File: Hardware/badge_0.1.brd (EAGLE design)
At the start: 100 x 50 mm, 59 parts, among them CON1 PH_2, IC1 CP2102, SW2 MK12C02, U1 SMBT2222A, U2 SMBT2222A, U4 MCP73832T-2DCI/OT

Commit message: Added optional connections to the anchors for the battery connector and slide switch To place on schematic, use the invoke tool
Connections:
- net GND: now also CON1.P$3, CON1.P$4, SW2.P$4, SW2.P$5, SW2.P$6, SW2.P$7
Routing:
- net GND: track 372.4 -> 379.8 mm, vias 114 -> 117
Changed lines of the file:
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@@
 <?xml version="1.0" encoding="utf-8"?>
 <!DOCTYPE eagle SYSTEM "eagle.dtd">
-<eagle version="7.5.0">
+<eagle version="7.1.0">
 <drawing>
 <settings>
@@
 <via x="48.10125" y="28.09875" extent="1-16" drill="0.4064" diameter="0.8128" shape="octagon"/>
 <wire x1="48.10125" y1="28.09875" x2="49.05375" y2="28.09875" width="0.8128" layer="1"/>
-<wire x1="61.595" y1="34.6075" x2="60.563125" y2="34.6075" width="0.8128" layer="1"/>
-<via x="60.563125" y="34.6075" extent="1-16" drill="0.635" shape="octagon"/>
-<wire x1="60.563125" y1="34.6075" x2="61.43625" y2="34.6075" width="0.8128" layer="16"/>
+<wire x1="61.595" y1="34.6075" x2="61.198125" y2="34.6075" width="0.8128" layer="1"/>
+<via x="61.198125" y="34.6075" extent="1-16" drill="0.635" shape="octagon"/>
+<wire x1="61.198125" y1="34.6075" x2="61.43625" y2="34.6075" width="0.8128" layer="16"/>
 <wire x1="61.43625" y1="34.6075" x2="61.595" y2="34.44875" width="0.8128" layer="16"/>
 <wire x1="74.93" y1="26.19375" x2="74.93" y2="22.70125" width="0.8128" layer="16"/>
 <via x="67.706875" y="6.985" extent="1-16" drill="0.635" shape="octagon"/>
-<polygon width="0.3048" layer="1" thermals="no">
-<vertex x="65.960625" y="10.00125"/>
-<vertex x="68.341875" y="10.00125"/>
-<vertex x="68.341875" y="6.429375"/>
-<vertex x="65.88125" y="6.429375"/>
-</polygon>
 <polygon width="0.254" layer="1">
 <vertex x="92.86875" y="44.92625"/>
@@
 <via x="9.128125" y="33.17875" extent="1-16" drill="0.635" shape="octagon"/>
 <wire x1="9.128125" y1="33.17875" x2="15.08125" y2="33.17875" width="0.8128" layer="16"/>
+<polygon width="0.3048" layer="1" isolate="0.2032" thermals="no" rank="2">
+<vertex x="0.238125" y="44.45"/>
+<vertex x="0.238125" y="35.56"/>
+<vertex x="5.87375" y="35.56"/>
+<vertex x="5.87375" y="44.45"/>
+</polygon>
+<contactref element="CON1" pad="P$3"/>
+<contactref element="CON1" pad="P$4"/>
+<polygon width="0.3048" layer="1" isolate="0.254" thermals="no" rank="3">
+<vertex x="61.198125" y="0.714375"/>
+<vertex x="61.198125" y="10.080625"/>
+<vertex x="69.37375" y="10.080625"/>
+<vertex x="69.37375" y="0.714375"/>
+</polygon>
+<contactref element="SW2" pad="P$4"/>
+<contactref element="SW2" pad="P$5"/>
+<contactref element="SW2" pad="P$6"/>
+<contactref element="SW2" pad="P$7"/>
+<wire x1="9.04875" y1="47.9425" x2="8.969375" y2="47.9425" width="0.3048" layer="1"/>
+<wire x1="8.969375" y1="47.9425" x2="7.46125" y2="46.434375" width="0.3048" layer="1"/>
+<wire x1="7.46125" y1="46.434375" x2="4.048125" y2="46.434375" width="0.3048" layer="1"/>
+<wire x1="4.048125" y1="46.434375" x2="3.01625" y2="45.4025" width="0.3048" layer="1"/>
+<wire x1="3.01625" y1="45.4025" x2="3.01625" y2="43.97375" width="0.3048" layer="1"/>
+<wire x1="3.01625" y1="43.97375" x2="3.095625" y2="43.894375" width="0.3048" layer="1"/>
+<via x="68.8975" y="6.985" extent="1-16" drill="0.635" shape="octagon"/>
+<via x="68.8975" y="8.255" extent="1-16" drill="0.635" shape="octagon"/>
+<via x="68.8975" y="9.525" extent="1-16" drill="0.635" shape="octagon"/>
 </signal>
 <signal name="GPIO12/SPI_SO">

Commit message: removed slant from lcd reset trace upon Yu Siang's rec
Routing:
- net RESET: track 178.0 -> 155.9 mm
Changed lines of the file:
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@@
 <?xml version="1.0" encoding="utf-8"?>
 <!DOCTYPE eagle SYSTEM "eagle.dtd">
-<eagle version="7.1.0">
+<eagle version="7.5.0">
 <drawing>
 <settings>
@@
 <contactref element="TP5" pad="TP"/>
 <via x="11.985625" y="21.11375" extent="1-16" drill="0.3048" shape="octagon"/>
-<wire x1="7.858" y1="19.98175" x2="9.035" y2="21.15875" width="0.3048" layer="1"/>
-<wire x1="7.858" y1="19.98175" x2="5.23875" y2="19.98175" width="0.3048" layer="1"/>
 <wire x1="5.23875" y1="27.4350625" x2="4.4163125" y2="27.4350625" width="0.3048" layer="1"/>
 <wire x1="4.4163125" y1="27.4350625" x2="4.1275" y2="27.14625" width="0.3048" layer="1"/>
@@
 <wire x1="53.2844375" y1="39.14775" x2="56.29275" y2="39.14775" width="0.3048" layer="1"/>
 <wire x1="56.29275" y1="39.14775" x2="57.070625" y2="39.925625" width="0.3048" layer="1"/>
-<wire x1="11.985625" y1="21.11375" x2="11.985625" y2="13.414375" width="0.4064" layer="1"/>
-<wire x1="11.985625" y1="13.414375" x2="16.271875" y2="9.128125" width="0.4064" layer="1"/>
-<wire x1="16.271875" y1="9.128125" x2="35.639375" y2="9.128125" width="0.4064" layer="1"/>
-<wire x1="35.639375" y1="9.128125" x2="36.83" y2="10.31875" width="0.4064" layer="1"/>
-<via x="36.83" y="10.31875" extent="1-16" drill="0.6" shape="square"/>
-<wire x1="36.83" y1="10.31875" x2="36.83" y2="27.543125" width="0.4064" layer="16"/>
 <wire x1="36.83" y1="27.543125" x2="35.56" y2="28.813125" width="0.4064" layer="16"/>
 <wire x1="35.56" y1="28.813125" x2="35.56" y2="29.606875" width="0.4064" layer="16"/>
@@
 <wire x1="57.070625" y1="39.925625" x2="57.070625" y2="40.64" width="0.3048" layer="1"/>
 <wire x1="57.070625" y1="40.64" x2="56.99125" y2="40.719375" width="0.3048" layer="1"/>
+<wire x1="9.035" y1="21.15875" x2="6.41575" y2="21.15875" width="0.4064" layer="1"/>
+<wire x1="6.41575" y1="21.15875" x2="5.23875" y2="19.98175" width="0.4064" layer="1"/>
+<wire x1="11.985625" y1="21.11375" x2="15.08125" y2="21.11375" width="0.4064" layer="1"/>
+<wire x1="15.08125" y1="21.11375" x2="16.271875" y2="22.304375" width="0.4064" layer="1"/>
+<wire x1="16.271875" y1="22.304375" x2="16.271875" y2="24.050625" width="0.4064" layer="1"/>
+<wire x1="16.271875" y1="24.050625" x2="17.4625" y2="25.24125" width="0.4064" layer="1"/>
+<wire x1="17.4625" y1="25.24125" x2="36.83" y2="25.24125" width="0.4064" layer="1"/>
+<via x="36.83" y="25.24125" extent="1-16" drill="0.3048" shape="octagon"/>
+<wire x1="36.83" y1="25.24125" x2="36.83" y2="27.543125" width="0.4064" layer="16"/>
 </signal>
 <signal name="ADC">

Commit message: increased power trace width
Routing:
- net 5V: track 78.2 -> 79.5 mm
- net GND: vias 117 -> 112
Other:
- outline, holes or cut-outs redrawn
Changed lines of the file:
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@@
 <board>
 <plain>
-<wire x1="57.2881125" y1="0" x2="97.46" y2="0" width="0.0635" layer="20"/>
+<wire x1="57.7643625" y1="0" x2="97.46" y2="0" width="0.0635" layer="20"/>
 <wire x1="97.46" y1="0" x2="100" y2="2.54" width="0.0635" layer="20" curve="90"/>
 <wire x1="100" y1="2.54" x2="100" y2="47.46" width="0.0635" layer="20"/>
@@
 <text x="20.0025" y="47.46625" size="0.6096" layer="21" font="vector" rot="R90" align="center">100R</text>
 <text x="18.811875" y="2.38125" size="0.6096" layer="21" font="vector" rot="R90" align="center">100R</text>
-<wire x1="56.03875" y1="0.47625" x2="56.03875" y2="4.92125" width="0.8128" layer="22"/>
-<wire x1="56.03875" y1="4.92125" x2="56.515" y2="5.3975" width="0.8128" layer="22"/>
-<wire x1="56.515" y1="5.3975" x2="56.515" y2="15.08125" width="0.8128" layer="22"/>
+<wire x1="56.515" y1="0.47625" x2="56.515" y2="15.08125" width="0.8128" layer="22"/>
 <wire x1="56.515" y1="15.08125" x2="57.30875" y2="15.875" width="0.8128" layer="22"/>
 <wire x1="57.30875" y1="15.875" x2="57.30875" y2="25.24125" width="0.8128" layer="22"/>
@@
 <wire x1="50.32375" y1="25.7175" x2="50.95875" y2="25.7175" width="0.127" layer="21"/>
 <wire x1="50.95875" y1="25.7175" x2="50.64125" y2="26.035" width="0.127" layer="21"/>
-<text x="51.27625" y="2.06375" size="2.1844" layer="22" font="vector" rot="MR0" align="center">X</text>
-<text x="53.975" y="2.69875" size="1.016" layer="22" font="vector" rot="SMR180" align="center">CTF</text>
+<text x="51.7525" y="2.06375" size="2.1844" layer="22" font="vector" rot="MR0" align="center">X</text>
+<text x="54.45125" y="2.69875" size="1.016" layer="22" font="vector" rot="SMR180" align="center">CTF</text>
 <text x="46.355" y="1.42875" size="1.016" layer="22" font="vector" rot="SMR180" align="center">CP2102</text>
 <text x="46.83125" y="2.69875" size="1.016" layer="22" font="vector" rot="SMR180" align="center">USB-TTL</text>
@@
 <wire x1="43.1403125" y1="25.24125" x2="43.1403125" y2="0.8128" width="0.0635" layer="20"/>
 <wire x1="43.1403125" y1="0.8128" x2="43.9531125" y2="0" width="0.0635" layer="20" curve="90"/>
-<wire x1="43.9531125" y1="0" x2="54.7893875" y2="0" width="0.0635" layer="20"/>
-<wire x1="54.7893875" y1="0" x2="55.6021875" y2="0.8128" width="0.0635" layer="20" curve="90"/>
-<wire x1="55.6021875" y1="0.8128" x2="55.6021875" y2="5.08" width="0.0635" layer="20"/>
-<wire x1="55.6021875" y1="5.08" x2="56.0784375" y2="5.55625" width="0.0635" layer="20"/>
-<wire x1="56.0784375" y1="5.55625" x2="56.0784375" y2="15.24" width="0.0635" layer="20"/>
+<wire x1="43.9531125" y1="0" x2="55.2656375" y2="0" width="0.0635" layer="20"/>
+<wire x1="55.2656375" y1="0" x2="56.0784375" y2="0.8128" width="0.0635" layer="20" curve="90"/>
+<wire x1="56.0784375" y1="0.8128" x2="56.0784375" y2="15.24" width="0.0635" layer="20"/>
 <wire x1="56.0784375" y1="15.24" x2="56.8721875" y2="16.03375" width="0.0635" layer="20"/>
 <wire x1="56.8721875" y1="16.03375" x2="56.8721875" y2="25.0825" width="0.0635" layer="20"/>
@@
 <wire x1="57.7453125" y1="25.4" x2="57.7453125" y2="15.71625" width="0.0635" layer="20"/>
 <wire x1="57.7453125" y1="15.71625" x2="56.9515625" y2="14.9225" width="0.0635" layer="20"/>
-<wire x1="56.9515625" y1="14.9225" x2="56.9515625" y2="5.23875" width="0.0635" layer="20"/>
-<wire x1="56.9515625" y1="5.23875" x2="56.4753125" y2="4.7625" width="0.0635" layer="20"/>
-<wire x1="56.4753125" y1="4.7625" x2="56.4753125" y2="0.8128" width="0.0635" layer="20"/>
-<wire x1="56.4753125" y1="0.8128" x2="57.2881125" y2="0" width="0.0635" layer="20" curve="90"/>
+<wire x1="56.9515625" y1="14.9225" x2="56.9515625" y2="0.8128" width="0.0635" layer="20"/>
+<wire x1="56.9515625" y1="0.8128" x2="57.7643625" y2="0" width="0.0635" layer="20" curve="90"/>
 <wire x1="49.05375" y1="25.9159375" x2="49.05375" y2="26.7890625" width="0.0635" layer="20" curve="180"/>
 <wire x1="52.86375" y1="26.7890625" x2="52.86375" y2="25.9159375" width="0.0635" layer="20" curve="180"/>
@@
 <via x="65.7225" y="20.79625" extent="1-16" drill="0.3048" shape="octagon"/>
 <via x="65.7225" y="20.0025" extent="1-16" drill="0.3048" shape="octagon"/>
-<via x="65.7225" y="19.20875" extent="1-16" drill="0.3048" shape="octagon"/>
 <via x="63.5" y="22.06625" extent="1-16" drill="0.3048" shape="octagon"/>
 <via x="63.5" y="22.70125" extent="1-16" drill="0.3048" shape="octagon"/>
@@
 <contactref element="U$14" pad="3"/>
 <polygon width="0.3048" layer="1" isolate="0.127" thermals="no">
-<vertex x="58.658125" y="16.1925"/>
+<vertex x="58.658125" y="15.795625"/>
 <vertex x="58.658125" y="7.62"/>
 <vertex x="63.261875" y="7.62"/>
@@
 <vertex x="64.373125" y="13.335"/>
 <vertex x="64.531875" y="13.49375"/>
-<vertex x="64.531875" y="16.1925"/>
+<vertex x="64.531875" y="15.795625"/>
 </polygon>
 <via x="67.071875" y="16.113125" extent="1-16" drill="0.635" shape="octagon"/>
 <via x="64.373125" y="15.39875" extent="1-16" drill="0.3048" shape="octagon"/>
-<via x="64.373125" y="16.03375" extent="1-16" drill="0.3048" shape="octagon"/>
-<via x="63.738125" y="16.03375" extent="1-16" drill="0.3048" shape="octagon"/>
-<via x="63.103125" y="16.03375" extent="1-16" drill="0.3048" shape="octagon"/>
 <via x="62.468125" y="15.39875" extent="1-16" drill="0.3048" shape="octagon"/>
-<via x="62.468125" y="16.03375" extent="1-16" drill="0.3048" shape="octagon"/>
 <via x="58.975625" y="14.2875" extent="1-16" drill="0.3048" shape="octagon"/>
 <via x="62.309375" y="13.97" extent="1-16" drill="0.3048" shape="octagon"/>
@@
 <via x="67.78625" y="23.97125" extent="1-16" drill="0.635" shape="octagon"/>
 <wire x1="67.78625" y1="23.97125" x2="67.78625" y2="18.494375" width="0.8128" layer="1"/>
-<wire x1="65.484375" y1="16.1925" x2="67.78625" y2="18.494375" width="0.8128" layer="1"/>
+<wire x1="65.484375" y1="16.1925" x2="65.7225" y2="16.430625" width="0.8128" layer="1"/>
+<wire x1="65.7225" y1="16.430625" x2="67.78625" y2="18.494375" width="0.8128" layer="1"/>
 <wire x1="48.41875" y1="45.4025" x2="46.355" y2="45.4025" width="0.8128" layer="1"/>
 <contactref element="LED1" pad="A"/>
@@
 <contactref element="U$9" pad="3"/>
 <wire x1="64.4398" y1="19.42465" x2="64.4398" y2="19.3802" width="0.3048" layer="1"/>
-<wire x1="64.4398" y1="19.3802" x2="65.24625" y2="18.57375" width="0.3048" layer="1"/>
-<wire x1="65.24625" y1="18.57375" x2="65.24625" y2="16.906875" width="0.3048" layer="1"/>
-<wire x1="65.24625" y1="16.906875" x2="65.008125" y2="16.66875" width="0.3048" layer="1"/>
-<wire x1="65.008125" y1="16.66875" x2="63.631875" y2="16.66875" width="0.3048" layer="1"/>
-<wire x1="63.631875" y1="16.66875" x2="62.520625" y2="17.700625" width="0.3048" layer="1"/>
 <wire x1="62.5602" y1="17.740425" x2="62.520625" y2="17.700625" width="0.4064" layer="1"/>
 <contactref element="U$9" pad="1"/>
 <contactref element="D2" pad="C"/>
 <wire x1="59.989375" y1="15.71625" x2="60.086875" y2="15.81375" width="0.8128" layer="1"/>
-<wire x1="60.086875" y1="15.81375" x2="60.63375" y2="15.81375" width="0.6096" layer="1"/>
-<wire x1="60.63375" y1="15.81375" x2="62.520625" y2="17.700625" width="0.6096" layer="1"/>
 <wire x1="62.5602" y1="19.42465" x2="62.5602" y2="17.7402" width="0.4064" layer="1"/>
 <wire x1="62.5602" y1="17.7402" x2="62.520625" y2="17.700625" width="0.4064" layer="1"/>
@@
 <wire x1="59.53125" y1="2.306875" x2="58.90125" y2="2.306875" width="0.8128" layer="1"/>
 <wire x1="58.90125" y1="2.306875" x2="58.89625" y2="2.301875" width="0.8128" layer="1"/>
+<wire x1="62.520625" y1="17.700625" x2="62.520625" y2="17.145" width="0.6096" layer="1"/>
+<wire x1="62.520625" y1="17.145" x2="62.520625" y2="17.013125" width="0.6096" layer="1"/>
+<wire x1="65.325625" y1="16.51" x2="65.643125" y2="16.51" width="0.6096" layer="1"/>
+<wire x1="65.643125" y1="16.51" x2="65.7225" y2="16.430625" width="0.6096" layer="1"/>
+<wire x1="64.4398" y1="19.3802" x2="64.677925" y2="19.3802" width="0.4064" layer="1"/>
+<wire x1="64.677925" y1="19.3802" x2="65.325625" y2="18.7325" width="0.4064" layer="1"/>
+<wire x1="65.325625" y1="18.7325" x2="65.325625" y2="16.51" width="0.4064" layer="1"/>
+<wire x1="60.086875" y1="15.81375" x2="61.189375" y2="15.81375" width="0.8128" layer="1"/>
+<wire x1="61.189375" y1="15.81375" x2="62.520625" y2="17.145" width="0.8128" layer="1"/>
+<wire x1="65.325625" y1="16.51" x2="63.02375" y2="16.51" width="0.8128" layer="1"/>
+<wire x1="63.02375" y1="16.51" x2="62.520625" y2="17.013125" width="0.8128" layer="1"/>
 </signal>
 <signal name="N$16">

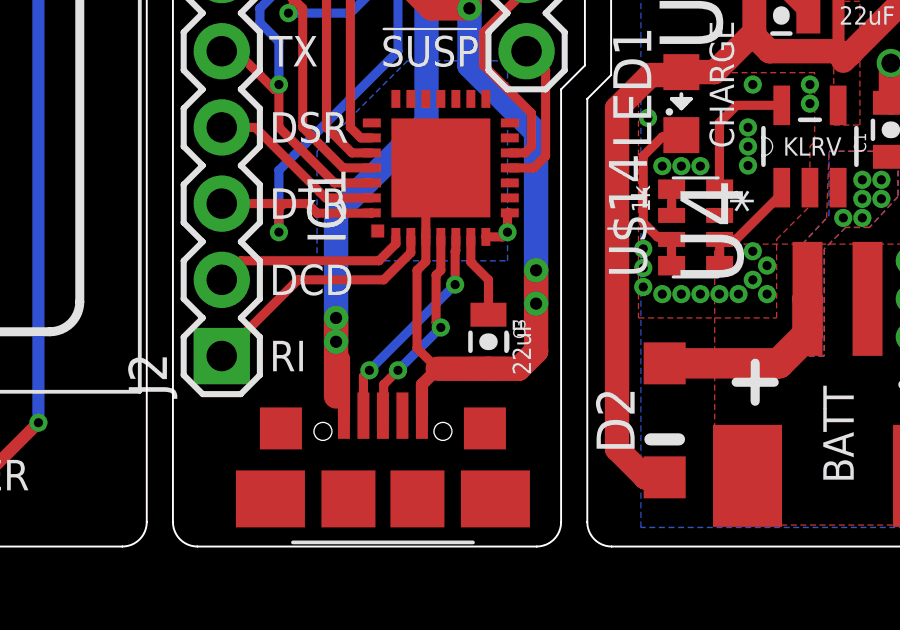
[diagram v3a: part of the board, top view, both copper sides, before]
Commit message: Added test points for USB data lines.
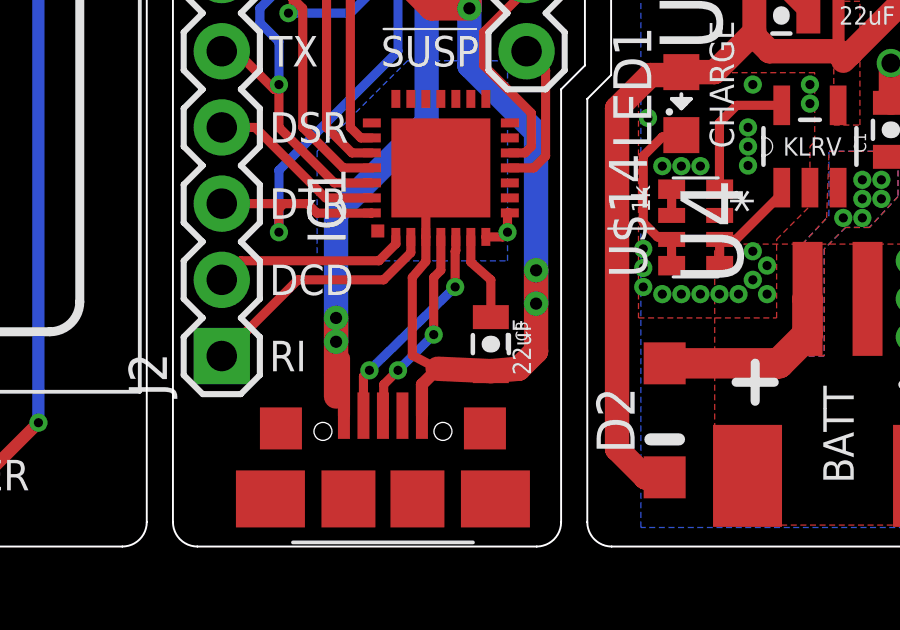
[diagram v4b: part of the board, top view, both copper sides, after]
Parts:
- moved C3 0.11 mm to (53.7, 6.75)
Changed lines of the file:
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@@
 <attribute name="PROD_ID" value="CONN-09696" x="54.9275" y="24.13" size="1.778" layer="27" rot="R270" display="off"/>
 </element>
-<element name="C3" library="SparkFun-Capacitors" package="0805-CAP" value="10uF" x="53.6575" y="6.82625" rot="R270"/>
+<element name="C3" library="SparkFun-Capacitors" package="0805-CAP" value="10uF" x="53.736875" y="6.746875" rot="R270"/>
 <element name="LED3" library="led" package="SML0805" value="" x="20.0025" y="6.19125"/>
 <element name="LED4" library="led" package="SML0805" value="" x="25.003125" y="6.19125"/>
@@
 <wire x1="51.57" y1="12.120625" x2="52.07" y2="12.620625" width="0.3048" layer="1"/>
 <wire x1="51.57" y1="10.320625" x2="51.57" y2="9.50125" width="0.3048" layer="1"/>
-<wire x1="51.57" y1="9.50125" x2="51.27625" y2="9.2075" width="0.3048" layer="1"/>
+<wire x1="51.57" y1="9.50125" x2="51.1175" y2="8.969375" width="0.3048" layer="1"/>
 <contactref element="U$14" pad="3"/>
 <polygon width="0.3048" layer="1" isolate="0.127" thermals="no">
@@
 <wire x1="51.44" y1="4.3625" x2="51.44" y2="5.4025" width="0.4064" layer="1"/>
 <wire x1="51.44" y1="5.4025" x2="51.96375" y2="5.92625" width="0.4064" layer="1"/>
-<wire x1="51.27625" y1="9.2075" x2="51.27625" y2="6.61375" width="0.3048" layer="1"/>
-<wire x1="51.27625" y1="6.61375" x2="51.96375" y2="5.92625" width="0.3048" layer="1"/>
-<wire x1="53.6575" y1="5.92625" x2="51.96375" y2="5.92625" width="0.8128" layer="1"/>
-<wire x1="53.6575" y1="5.92625" x2="54.6625" y2="5.92625" width="0.8128" layer="1"/>
+<wire x1="51.1175" y1="8.969375" x2="51.1175" y2="6.375625" width="0.3048" layer="1"/>
+<wire x1="51.1175" y1="6.375625" x2="51.96375" y2="5.92625" width="0.3048" layer="1"/>
+<wire x1="53.736875" y1="5.846875" x2="51.96375" y2="5.92625" width="0.8128" layer="1"/>
+<wire x1="53.736875" y1="5.846875" x2="54.6625" y2="5.92625" width="0.8128" layer="1"/>
 <wire x1="54.6625" y1="5.92625" x2="55.245" y2="6.50875" width="0.8128" layer="1"/>
 <wire x1="5.23875" y1="31.141875" x2="5.23875" y2="32.385" width="0.8128" layer="1"/>
@@
 <wire x1="49.49" y1="4.3625" x2="49.49" y2="5.675" width="0.3048" layer="1"/>
 <via x="49.68875" y="5.87375" extent="1-16" drill="0.3048" shape="octagon"/>
-<via x="52.54625" y="8.73125" extent="1-16" drill="0.3048" shape="octagon"/>
-<wire x1="52.54625" y1="8.73125" x2="52.54625" y2="9.8425" width="0.3048" layer="1"/>
+<via x="52.54625" y="8.651875" extent="1-16" drill="0.3048" shape="octagon" alwaysstop="yes"/>
+<wire x1="52.54625" y1="8.651875" x2="52.54625" y2="9.8425" width="0.3048" layer="1"/>
 <wire x1="52.57" y1="10.320625" x2="52.57" y2="9.86625" width="0.3048" layer="1"/>
 <wire x1="52.57" y1="9.86625" x2="52.54625" y2="9.8425" width="0.3048" layer="1"/>
-<wire x1="49.68875" y1="5.87375" x2="52.54625" y2="8.73125" width="0.3048" layer="16"/>
+<wire x1="49.68875" y1="5.87375" x2="52.54625" y2="8.651875" width="0.3048" layer="16"/>
 <wire x1="49.49" y1="5.675" x2="49.68875" y2="5.87375" width="0.3048" layer="1"/>
 </signal>
@@
 <contactref element="IC1" pad="4"/>
 <wire x1="52.07" y1="10.320625" x2="52.07" y2="9.2075" width="0.3048" layer="1"/>
-<wire x1="52.07" y1="9.2075" x2="51.91125" y2="9.04875" width="0.3048" layer="1"/>
-<via x="52.07" y="7.3025" extent="1-16" drill="0.3048" shape="octagon"/>
+<wire x1="52.07" y1="9.2075" x2="51.831875" y2="8.969375" width="0.3048" layer="1"/>
+<via x="51.831875" y="7.064375" extent="1-16" drill="0.3048" shape="octagon" alwaysstop="yes"/>
 <via x="50.64125" y="5.87375" extent="1-16" drill="0.3048" shape="octagon"/>
 <wire x1="50.165" y1="5.3975" x2="50.165" y2="4.2875" width="0.3048" layer="1"/>
 <wire x1="50.165" y1="4.2875" x2="50.14" y2="4.3625" width="0.3048" layer="1"/>
-<wire x1="51.91125" y1="9.04875" x2="51.91125" y2="7.46125" width="0.3048" layer="1"/>
-<wire x1="51.91125" y1="7.46125" x2="52.07" y2="7.3025" width="0.3048" layer="1"/>
-<wire x1="52.07" y1="7.3025" x2="50.64125" y2="5.87375" width="0.3048" layer="16"/>
+<wire x1="51.831875" y1="8.969375" x2="51.831875" y2="7.064375" width="0.3048" layer="1"/>
+<wire x1="51.831875" y1="7.064375" x2="50.64125" y2="5.87375" width="0.3048" layer="16"/>
 <wire x1="50.64125" y1="5.87375" x2="50.165" y2="5.3975" width="0.3048" layer="1"/>
 </signal>
@@
 <contactref element="C3" pad="1"/>
 <wire x1="53.07" y1="10.320625" x2="53.07" y2="9.4775" width="0.3048" layer="1"/>
-<wire x1="53.07" y1="9.4775" x2="53.6575" y2="8.89" width="0.3048" layer="1"/>
-<wire x1="53.6575" y1="8.89" x2="53.6575" y2="7.72625" width="0.3048" layer="1"/>
+<wire x1="53.07" y1="9.4775" x2="53.736875" y2="8.89" width="0.3048" layer="1"/>
+<wire x1="53.736875" y1="8.89" x2="53.736875" y2="7.646875" width="0.3048" layer="1"/>
 </signal>
 <signal name="LCD_BL">
